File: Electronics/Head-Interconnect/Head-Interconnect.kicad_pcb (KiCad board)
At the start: 2 copper layers, 55 x 54.5 mm, 18 parts, among them J1 Conn_Coaxial, J2 Conn_02x03_Odd_Even

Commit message: Head interconnect finished
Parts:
- removed D1, D2: LED, LED_SMD:LED_0805_2012Metric_Pad1.15x1.40mm_HandSolder
- removed J1: Conn_Coaxial, Custom:SMA
- removed R1, R2: R, Resistor_SMD:R_0805_2012Metric_Pad1.15x1.40mm_HandSolder
- removed REF** (x4): MountingHole_3.2mm_M3_Pad_Via, MountingHole:MountingHole_3.2mm_M3_Pad_Via
- added H1: MountingHole_Pad, MountingHole:MountingHole_3.2mm_M3_Pad_Via, F.Cu at (126.4, 101.4)
- added H2: MountingHole_Pad, MountingHole:MountingHole_3.2mm_M3_Pad_Via, F.Cu at (126.4, 113.6)
- added H3: MountingHole_Pad, MountingHole:MountingHole_3.2mm_M3_Pad_Via, F.Cu at (168.6, 101.4)
- added H4: MountingHole_Pad, MountingHole:MountingHole_3.2mm_M3_Pad_Via, F.Cu at (168.6, 113.6)
- added J3: Conn_Coaxial, Connector_Coaxial:MMCX_Molex_73415-1471_Vertical, F.Cu at (161.3, 105.0)
- added J4: Conn_01x04_MountingPin, Connector_FFC-FPC:TE_84953-4_1x04-1MP_P1.0mm_Horizontal, F.Cu at (168.5, 85.9)
- added J5: Conn_Coaxial, Connector_Coaxial:MMCX_Molex_73415-1471_Vertical, F.Cu at (165.3, 91.8)
- added J6: Conn_01x04, Connector_PinSocket_2.54mm:PinSocket_1x04_P2.54mm_Vertical, F.Cu at (160.9, 97.4)
- added J7: Conn_01x20_MountingPin, Connector_FFC-FPC:TE_2-84953-0_1x20-1MP_P1.0mm_Horizontal, F.Cu at (175.3, 106.2)
- added JP1: Jumper, Jumper:SolderJumper-2_P1.3mm_Open_TrianglePad1.0x1.5mm, F.Cu at (165.6, 106.3)
- added JP2: Jumper, Jumper:SolderJumper-2_P1.3mm_Open_TrianglePad1.0x1.5mm, F.Cu at (169.1, 108.2)
- added JP3: Jumper, Jumper:SolderJumper-2_P1.3mm_Open_TrianglePad1.0x1.5mm, F.Cu at (166.4, 96.7)
- added JP4: Jumper, Jumper:SolderJumper-2_P1.3mm_Open_TrianglePad1.0x1.5mm, F.Cu at (161.6, 110.5)
- added LOGO1: Logo_Open_Hardware_Small, Symbol:OSHW-Symbol_6.7x6mm_SilkScreen, F.Cu at (152.7, 102.2)
- added TP6: TestPoint, TestPoint:TestPoint_THTPad_D1.0mm_Drill0.5mm, F.Cu at (140.0, 108.5)
- added TP7: TestPoint, TestPoint:TestPoint_THTPad_D1.0mm_Drill0.5mm, F.Cu at (131.7, 112.3)
- added TP8: TestPoint, TestPoint:TestPoint_THTPad_D1.0mm_Drill0.5mm, F.Cu at (134.9, 96.5)
- J2: footprint Custom:board-to-board -> Connector_PinSocket_1.27mm:PinSocket_2x03_P1.27mm_Vertical_SMD
- moved J2 14.8 mm to (162.2, 116.1), turned to 270 degrees
- moved R3 5.50 mm to (157.1, 105.0)
- moved C1 1.96 mm to (144.6, 103.0)
- moved C2 1.58 mm to (135.0, 103.0)
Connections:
- net +15V renamed /analog_+15V
- net -15V renamed /analog_-15V
- net GND renamed /analog_gnd
- J2 pad 1: Net-(J2-Pad1) -> /piezo_x-
- J2 pad 2: Net-(J2-Pad2) -> /piezo_x+
- J2 pad 3: Net-(J2-Pad3) -> /piezo_y+
- J2 pad 4: Net-(J2-Pad4) -> /piezo_gnd
- J2 pad 5: Net-(J2-Pad5) -> /piezo_y-
- J2 pad 6: Net-(J2-Pad6) -> /piezo_gnd
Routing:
- net /Stepper_A2: track 0.00 -> 29.0 mm, vias 0 -> 1
- net /Stepper_B2: track 0.00 -> 29.0 mm, vias 0 -> 1
- net /piezo_y-: track 0.00 -> 27.5 mm, vias 0 -> 2
- net /tunnel_gnd: track 0.00 -> 24.8 mm
- net /Stepper_B1: track 0.00 -> 24.7 mm, vias 0 -> 1
- net /piezo_y+: track 0.00 -> 21.8 mm, vias 0 -> 2
- net /Stepper_A1: track 0.00 -> 20.7 mm, vias 0 -> 1
- net /bias: track 0.00 -> 17.5 mm
- net /piezo_x-: track 0.00 -> 16.6 mm
- net /piezo_x+: track 0.00 -> 12.5 mm
- net /analog_-15V: track 0.00 -> 11.9 mm, vias 0 -> 8
- net /analog_+15V: track 0.00 -> 9.80 mm, vias 0 -> 8
- net /tunnel_gnd_ffc: track 0.00 -> 9.23 mm
- net /tunnel_signal_ffc: track 0.00 -> 8.81 mm
- net /piezo_gnd: track 0.00 -> 8.35 mm, vias 0 -> 3
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- added copper zone on B.Cu, net /analog_+15V
- added copper zone on F.Cu, net /analog_+15V
- added copper zone on B.Cu, net /analog_-15V
- added copper zone on F.Cu, net /analog_-15V
- added copper zone on B.Cu, net /analog_gnd
- added copper zone on F.Cu, net /analog_gnd
- added copper zone on F.Cu, net /bias_gnd
- added copper zone on B.Cu, net /piezo_gnd
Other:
- board size 55 x 54.5 mm -> 62 x 42.1 mm
- board text added: "Bias"
- board text added: "GND"
- board text added: "Gnd"
- board text added: "Piezo"
- board text added: "STM Head Interconnect"
- board text added: "Shield"
- board text added: "Sig"
- board text added: "Stepper"
- board text added: "Tunnel Current"
- board text added: "©mrkenhoff 2020"

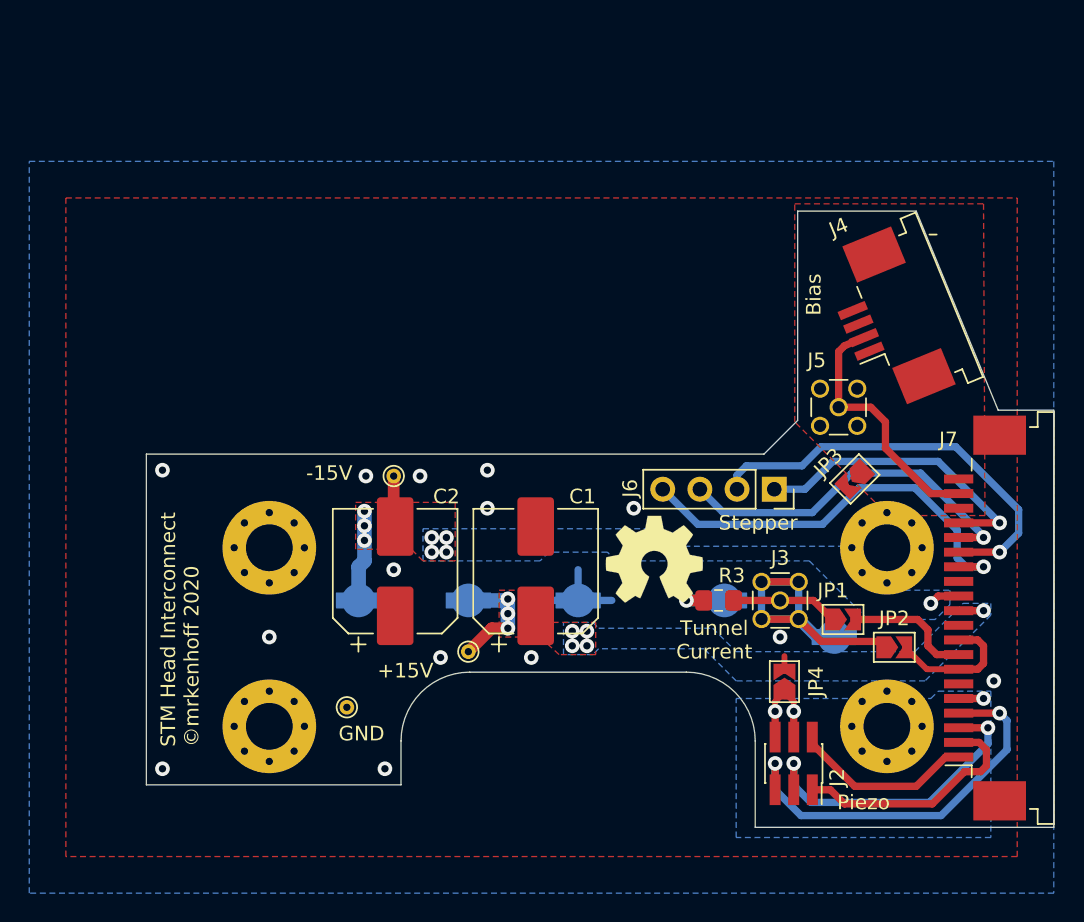
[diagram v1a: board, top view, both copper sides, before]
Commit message: Base interconnect and head interconnect in fabrication
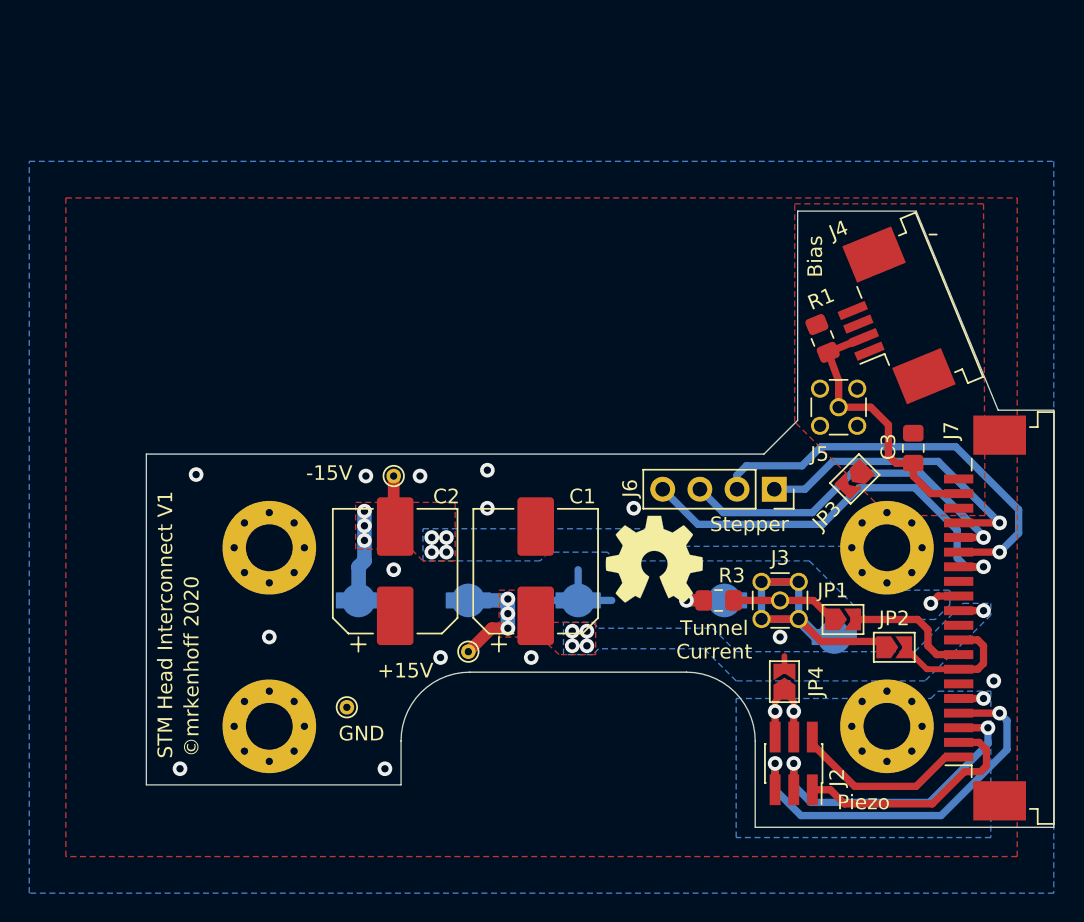
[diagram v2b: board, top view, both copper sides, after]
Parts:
- added C3: opt, Capacitor_SMD:C_0805_2012Metric_Pad1.15x1.40mm_HandSolder, F.Cu at (170.4, 94.6)
- added R1: opt, Resistor_SMD:R_0805_2012Metric_Pad1.15x1.40mm_HandSolder, F.Cu at (164.2, 87.1)
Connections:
- net /Stepper_A1 renamed /Stepper_A-
- net /Stepper_A2 renamed /Stepper_A+
- net /Stepper_B1 renamed /Stepper_B+
- net /Stepper_B2 renamed /Stepper_B-
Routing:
- net /bias: track 17.5 -> 18.9 mm
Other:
- board text added: "STM Head Interconnect V1"
- board text removed: "STM Head Interconnect"

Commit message: Added images
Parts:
- C1, C2: value CP -> 220u 35V
- TP1, TP2, TP3, TP4, TP5: value TestPoint -> 0905-0-15-20-75-14-11-0

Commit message: Added sample-bias interconnect and base interconnect V2
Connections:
- J6 pad 1: /Stepper_A- -> /Stepper_B+
- J6 pad 2: /Stepper_A+ -> /Stepper_B-
- J6 pad 3: /Stepper_B+ -> /Stepper_A-
- J6 pad 4: /Stepper_B- -> /Stepper_A+
- J7 pad 14: /Stepper_B- -> /Stepper_A+
- J7 pad 15: /Stepper_A+ -> /Stepper_B-
- J7 pad 16: /Stepper_B+ -> /Stepper_A-
- J7 pad 17: /Stepper_A- -> /Stepper_B+
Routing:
- net /Stepper_B+: track 24.7 -> 20.7 mm
- net /Stepper_A-: track 20.7 -> 24.7 mm

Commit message: Added value to R3 on head interconnect
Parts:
- R3: value R -> 49R9
